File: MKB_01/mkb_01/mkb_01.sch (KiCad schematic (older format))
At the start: 377 parts, among them J1 USB_C_Receptacle_USB2.0, J2 SW_Push, K1 SW_Push, M1 SW_Push, P1 SW_Push, Q1 SW_Push, Q2 BSP318, Q3 BSP318, T1 SW_Push, U1 LD1117S33TR_SOT223, U2 STM32F070CBTx, U3 SW_Push, X1 SW_Push, Y1 SW_Push, Y2 Crystal

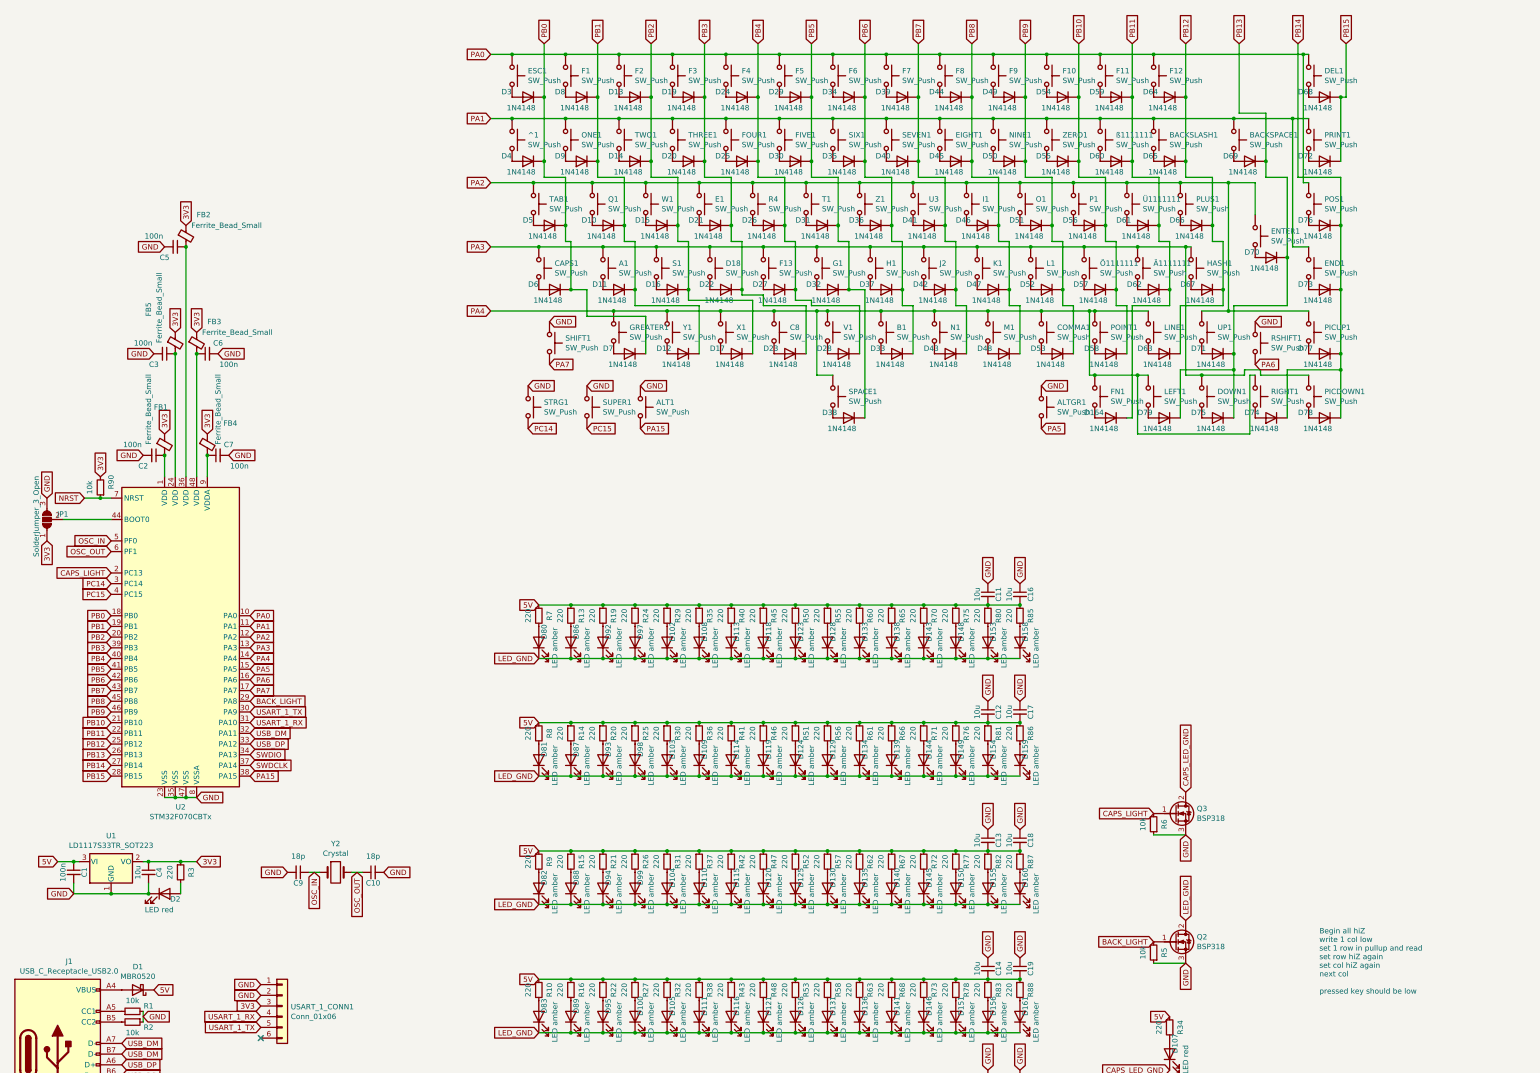
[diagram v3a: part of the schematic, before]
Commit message: change diode direction to read from column rather than rows, added some more caps for the mcu, updated BOM
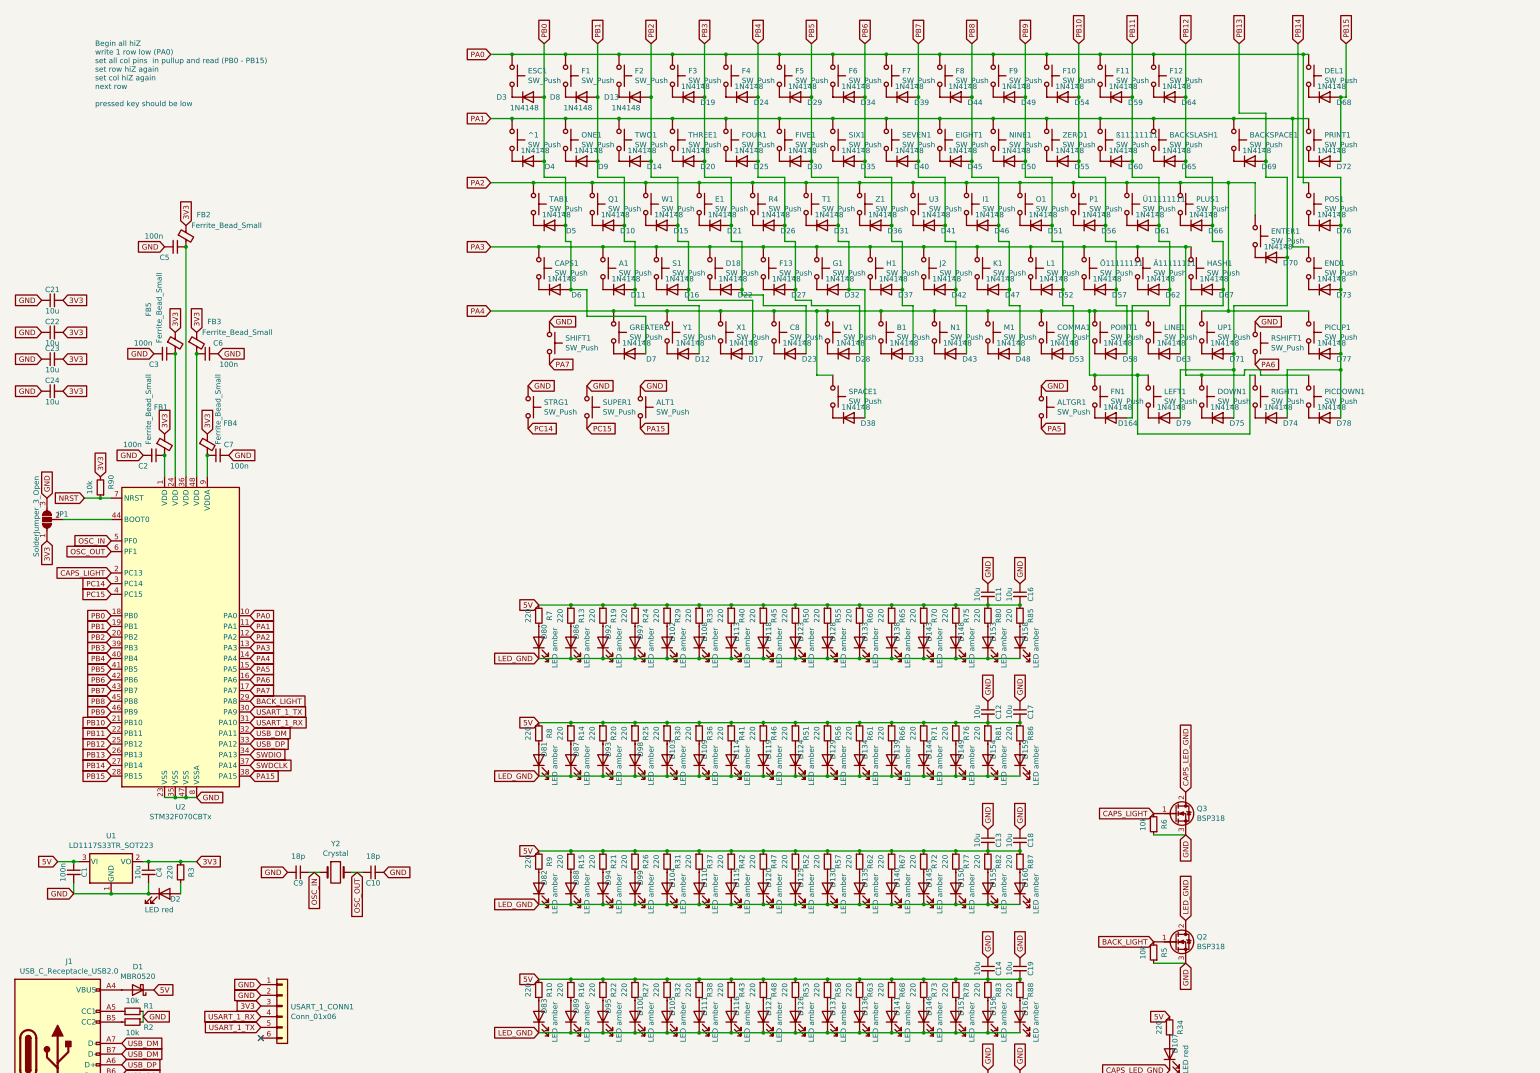
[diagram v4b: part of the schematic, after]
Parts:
- added C21, C22, C23, C24: 10u, Capacitor_SMD:C_0603_1608Metric_Pad1.08x0.95mm_HandSolder, symbol Device:C_Small
- renumbered Ä1111111 to Ä11111111, Ö1111111 to Ö11111111, Ü1111111 to Ü11111111, ß1111111 to ß11111111
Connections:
- net 3V3: now also C21.2, C22.2, C23.2, C24.2
- net GND: now also C21.1, C22.1, C23.1, C24.1
- net PB0: now also D3.2 (A), D4.2 (A), D5.2 (A), D6.2 (A), D7.2 (A); no longer D3.1 (K), D4.1 (K), D5.1 (K), D6.1 (K), D7.1 (K)
- net PB1: now also D10.2 (A), D11.2 (A), D12.2 (A), D8.2 (A), D9.2 (A); no longer D10.1 (K), D11.1 (K), D12.1 (K), D8.1 (K), D9.1 (K)
- net PB10: now also D54.2 (A), D55.2 (A), D56.2 (A), D57.2 (A), D58.2 (A); no longer D54.1 (K), D55.1 (K), D56.1 (K), D57.1 (K), D58.1 (K)
- net PB11: now also D164.2 (A), D59.2 (A), D60.2 (A), D61.2 (A), D62.2 (A); no longer D164.1 (K), D59.1 (K), D60.1 (K), D61.1 (K), D62.1 (K)
- net PB12: now also D63.2 (A), D64.2 (A), D65.2 (A), D66.2 (A), D67.2 (A); no longer D63.1 (K), D64.1 (K), D65.1 (K), D66.1 (K), D67.1 (K)
- net PB13: now also D69.2 (A), D70.2 (A), D71.2 (A), D75.2 (A), D79.2 (A); no longer D69.1 (K), D70.1 (K), D71.1 (K), D75.1 (K), D79.1 (K)
- net PB14: now also D73.2 (A), D74.2 (A), D76.2 (A), D77.2 (A), D78.2 (A); no longer D73.1 (K), D74.1 (K), D76.1 (K), D77.1 (K), D78.1 (K)
- net PB15: now also D68.2 (A), D72.2 (A); no longer D68.1 (K), D72.1 (K)
- net PB2: now also D13.2 (A), D14.2 (A), D15.2 (A), D16.2 (A), D17.2 (A); no longer D13.1 (K), D14.1 (K), D15.1 (K), D16.1 (K), D17.1 (K)
- net PB3: now also D19.2 (A), D20.2 (A), D21.2 (A), D22.2 (A), D23.2 (A); no longer D19.1 (K), D20.1 (K), D21.1 (K), D22.1 (K), D23.1 (K)
- net PB4: now also D24.2 (A), D25.2 (A), D26.2 (A), D27.2 (A), D28.2 (A); no longer D24.1 (K), D25.1 (K), D26.1 (K), D27.1 (K), D28.1 (K)
- net PB5: now also D29.2 (A), D30.2 (A), D31.2 (A), D32.2 (A), D38.2 (A); no longer D29.1 (K), D30.1 (K), D31.1 (K), D32.1 (K), D38.1 (K)
- net PB6: now also D33.2 (A), D34.2 (A), D35.2 (A), D36.2 (A), D37.2 (A); no longer D33.1 (K), D34.1 (K), D35.1 (K), D36.1 (K), D37.1 (K)
- net PB7: now also D39.2 (A), D40.2 (A), D41.2 (A), D42.2 (A), D43.2 (A); no longer D39.1 (K), D40.1 (K), D41.1 (K), D42.1 (K), D43.1 (K)
- net PB8: now also D44.2 (A), D45.2 (A), D46.2 (A), D47.2 (A), D48.2 (A); no longer D44.1 (K), D45.1 (K), D46.1 (K), D47.1 (K), D48.1 (K)
- net PB9: now also D49.2 (A), D50.2 (A), D51.2 (A), D52.2 (A), D53.2 (A); no longer D49.1 (K), D50.1 (K), D51.1 (K), D52.1 (K), D53.1 (K)
- net at ESC1.2: now also D3.1 (K); no longer D3.2 (A)
- net at F1.2: now also D8.1 (K); no longer D8.2 (A)
- net at F2.2: now also D13.1 (K); no longer D13.2 (A)
- net at F3.2: now also D19.1 (K); no longer D19.2 (A)
- net at F4.2: now also D24.1 (K); no longer D24.2 (A)
- net at F5.2: now also D29.1 (K); no longer D29.2 (A)
- net at F6.2: now also D34.1 (K); no longer D34.2 (A)
- net at F7.2: now also D39.1 (K); no longer D39.2 (A)
- net at F8.2: now also D44.1 (K); no longer D44.2 (A)
- net at F9.2: now also D49.1 (K); no longer D49.2 (A)
- net at F10.2: now also D54.1 (K); no longer D54.2 (A)
- net at F11.2: now also D59.1 (K); no longer D59.2 (A)
- net at F12.2: now also D64.1 (K); no longer D64.2 (A)
- net at DEL1.2: now also D68.1 (K); no longer D68.2 (A)
- net at PRINT1.2: now also D72.1 (K); no longer D72.2 (A)
- net at POS1.2: now also D76.1 (K); no longer D76.2 (A)
- net at ^1.2: now also D4.1 (K); no longer D4.2 (A)
- net at ONE1.2: now also D9.1 (K); no longer D9.2 (A)
- net at TWO1.2: now also D14.1 (K); no longer D14.2 (A)
- net at THREE1.2: now also D20.1 (K); no longer D20.2 (A)
- net at FOUR1.2: now also D25.1 (K); no longer D25.2 (A)
- net at FIVE1.2: now also D30.1 (K); no longer D30.2 (A)
- net at SIX1.2: now also D35.1 (K); no longer D35.2 (A)
- net at SEVEN1.2: now also D40.1 (K); no longer D40.2 (A)
- net at EIGHT1.2: now also D45.1 (K); no longer D45.2 (A)
- net at NINE1.2: now also D50.1 (K); no longer D50.2 (A)
- net at ZERO1.2: now also D55.1 (K); no longer D55.2 (A)
- net at ß11111111.2: now also D60.1 (K); no longer D60.2 (A)
- net at BACKSLASH1.2: now also D65.1 (K); no longer D65.2 (A)
- net at BACKSPACE1.2: now also D69.1 (K); no longer D69.2 (A)
- net at END1.2: now also D73.1 (K); no longer D73.2 (A)
- net at PICUP1.2: now also D77.1 (K); no longer D77.2 (A)
- net at TAB1.2: now also D5.1 (K); no longer D5.2 (A)
- net at Q1.2: now also D10.1 (K); no longer D10.2 (A)
- net at W1.2: now also D15.1 (K); no longer D15.2 (A)
- net at E1.2: now also D21.1 (K); no longer D21.2 (A)
- net at R4.2: now also D26.1 (K); no longer D26.2 (A)
- net at T1.2: now also D31.1 (K); no longer D31.2 (A)
- net at Z1.2: now also D36.1 (K); no longer D36.2 (A)
- net at U3.2: now also D41.1 (K); no longer D41.2 (A)
- net at I1.2: now also D46.1 (K); no longer D46.2 (A)
- net at O1.2: now also D51.1 (K); no longer D51.2 (A)
- net at P1.2: now also D56.1 (K); no longer D56.2 (A)
- net at Ü11111111.2: now also D61.1 (K); no longer D61.2 (A)
- net at PLUS1.2: now also D66.1 (K); no longer D66.2 (A)
- net at ENTER1.2: now also D70.1 (K); no longer D70.2 (A)
- net at RIGHT1.2: now also D74.1 (K); no longer D74.2 (A)
- net at PICDOWN1.2: now also D78.1 (K); no longer D78.2 (A)
- net at CAPS1.2: now also D6.1 (K); no longer D6.2 (A)
- net at A1.2: now also D11.1 (K); no longer D11.2 (A)
- net at S1.2: now also D16.1 (K); no longer D16.2 (A)
- net at D18.2: now also D22.1 (K); no longer D22.2 (A)
- net at F13.2: now also D27.1 (K); no longer D27.2 (A)
- net at G1.2: now also D32.1 (K); no longer D32.2 (A)
- net at H1.2: now also D37.1 (K); no longer D37.2 (A)
- net at J2.2: now also D42.1 (K); no longer D42.2 (A)
- net at K1.2: now also D47.1 (K); no longer D47.2 (A)
- net at L1.2: now also D52.1 (K); no longer D52.2 (A)
- net at Ö11111111.2: now also D57.1 (K); no longer D57.2 (A)
- net at Ä11111111.2: now also D62.1 (K); no longer D62.2 (A)
- net at HASH1.2: now also D67.1 (K); no longer D67.2 (A)
- net at UP1.2: now also D71.1 (K); no longer D71.2 (A)
- net at DOWN1.2: now also D75.1 (K); no longer D75.2 (A)
- net at LEFT1.2: now also D79.1 (K); no longer D79.2 (A)
- net at GREATER1.2: now also D7.1 (K); no longer D7.2 (A)
- net at Y1.2: now also D12.1 (K); no longer D12.2 (A)
- net at X1.2: now also D17.1 (K); no longer D17.2 (A)
- net at C8.2: now also D23.1 (K); no longer D23.2 (A)
- net at V1.2: now also D28.1 (K); no longer D28.2 (A)
- net at B1.2: now also D33.1 (K); no longer D33.2 (A)
- net at SPACE1.2: now also D38.1 (K); no longer D38.2 (A)
- net at N1.2: now also D43.1 (K); no longer D43.2 (A)
- net at M1.2: now also D48.1 (K); no longer D48.2 (A)
- net at COMMA1.2: now also D53.1 (K); no longer D53.2 (A)
- net at POINT1.2: now also D58.1 (K); no longer D58.2 (A)
- net at LINE1.2: now also D63.1 (K); no longer D63.2 (A)
- net at FN1.2: now also D164.1 (K); no longer D164.2 (A)
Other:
- note added: "Begin all hiZ\nwrite 1 row low (PA0)\nset all col pins in pullup and read (PB0 - PB15)\nset row hiZ again\nset col hiZ again\nnext row\n\npressed key should be low"
- note removed: "Begin all hiZ\nwrite 1 col low\nset 1 row in pullup and read\nset row hiZ again\nset col hiZ again\nnext col\n\npressed key should be low"
